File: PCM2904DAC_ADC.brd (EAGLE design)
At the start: 85 x 56 mm, 48 parts, among them IC1 LM358D, Q1 12MHz, X1 V+, D-, D+, GND

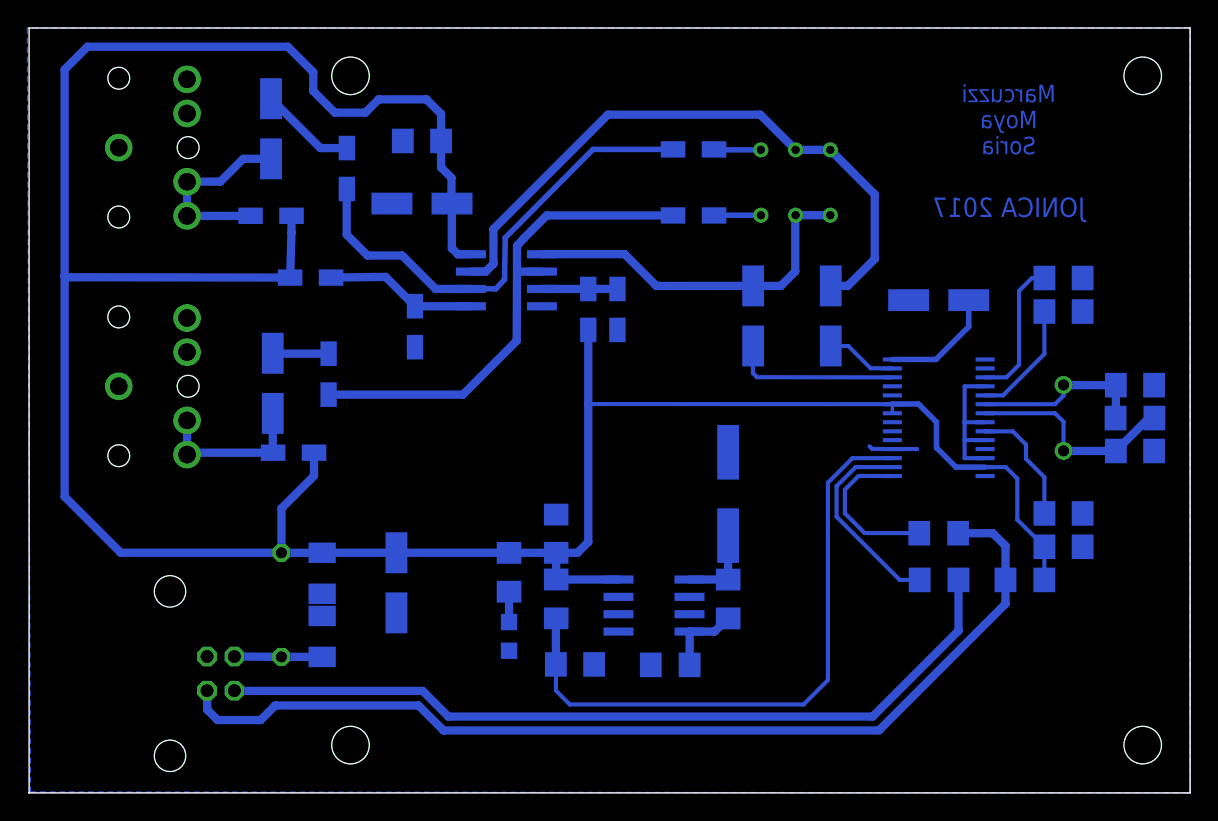
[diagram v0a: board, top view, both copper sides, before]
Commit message: Mirror + R 100 Ohms
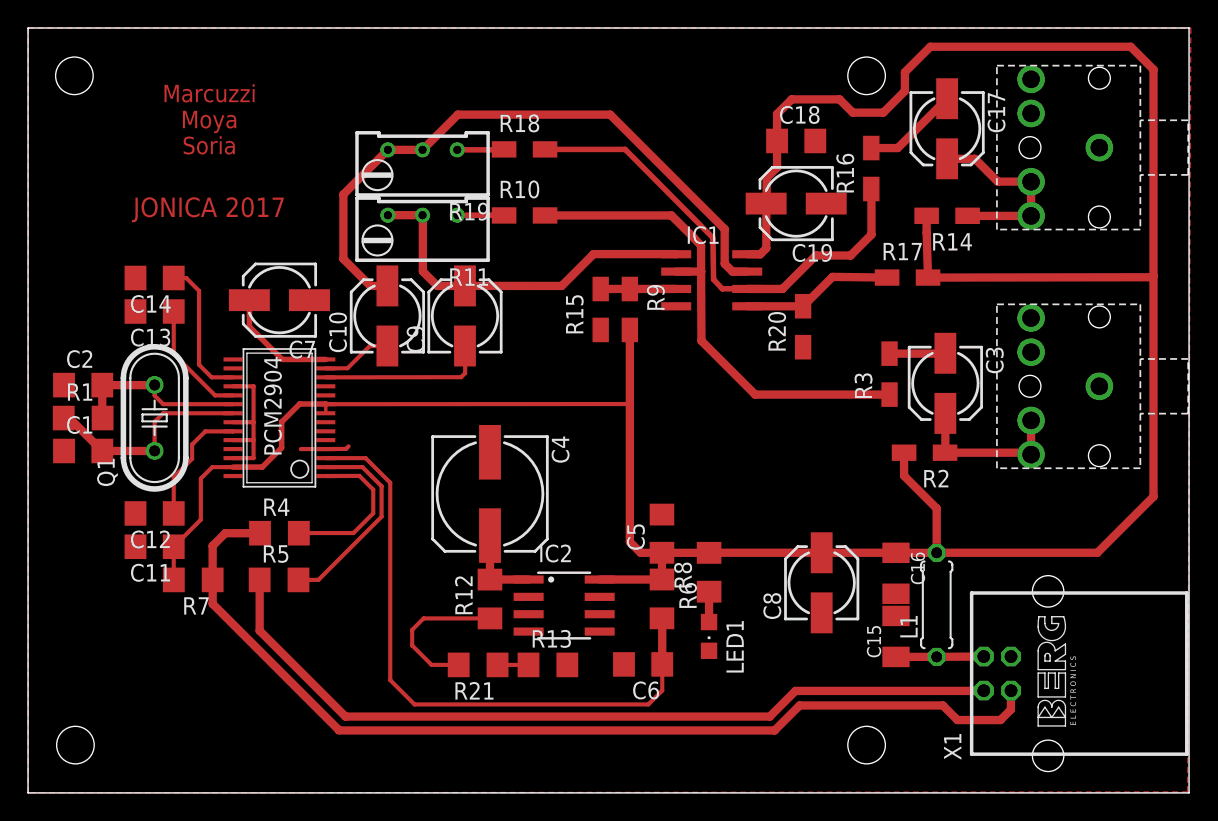
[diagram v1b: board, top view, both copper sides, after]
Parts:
- added R21: 100, rcl:R1206
- R12: value 5k7 -> 5k6
- moved C1 77.0 mm to (3.93, 25.0), flipped to the top
- moved C2 77.0 mm to (3.93, 29.9), flipped to the top
- moved R1 77.0 mm to (3.93, 27.4), flipped to the top
- moved U$1 71.8 mm to (78.3, 47.2), flipped to the top
- moved U$8 71.8 mm to (78.3, 29.8), flipped to the top
- moved C11 66.5 mm to (9.16, 18.0), flipped to the top
- moved C12 66.5 mm to (9.16, 20.5), flipped to the top
- moved C13 66.5 mm to (9.16, 35.2), flipped to the top
- moved C14 66.5 mm to (9.16, 37.7), flipped to the top
- moved Q1 66.5 mm to (9.16, 27.5), flipped to the top
- moved X1 64.3 mm to (74.6, 8.74), flipped to the top
- moved R7 60.9 mm to (12.0, 15.6), flipped to the top
- moved C17 49.5 mm to (67.2, 48.6), flipped to the top
- moved R14 49.5 mm to (67.2, 42.3), flipped to the top
- moved C3 49.2 mm to (67.1, 30.0), flipped to the top
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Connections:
- removed net N$41: IC2.4, R12.1, R13.1
- new net N$26: R12.1, R21.2
- new net N$27: IC2.4, R13.1, R21.1
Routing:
- net N$26: track 0.00 -> 11.2 mm
- net N$41: track 5.66 -> 0.00 mm
- net N$27: track 0.00 -> 3.51 mm
- added copper zone on layer 1, net GND
- removed copper zone on layer 16, net GND
